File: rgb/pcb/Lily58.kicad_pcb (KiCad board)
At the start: 2 copper layers, 142.5 x 106.3 mm, 117 parts, among them J1 LED, J2 4PIN, P1 i2c_pin, P2 i2c_pin, P3 ICSP, P4 OLED, SW1 SW_PUSH, SW10 SW_PUSH, SW11 SW_PUSH, SW12 SW_PUSH, SW13 SW_PUSH, SW14 SW_PUSH, SW15 SW_PUSH, SW16 SW_PUSH, SW17 SW_PUSH, SW18 SW_PUSH, SW19 SW_PUSH, SW2 SW_PUSH, SW20 SW_PUSH, SW21 SW_PUSH, SW22 SW_PUSH, SW23 SW_PUSH, SW24 SW_PUSH, SW25 SW_PUSH, SW26 SW_PUSH, SW27 SW_PUSH, SW28 SW_PUSH, SW29 SW_PUSH, SW3 SW_PUSH, SW4 SW_PUSH, SW5 SW_PUSH, SW6 SW_PUSH, SW7 SW_PUSH, SW8 SW_PUSH, SW9 SW_PUSH, U1 ProMicro

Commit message: Add underglow
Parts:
- added L30: SK6812mini, Lily58-footprint:SK6812MINI_underglow_rev, F.Cu at (120.5, 60.2)
- added L31: SK6812mini, Lily58-footprint:SK6812MINI_underglow_rev, F.Cu at (158.6, 56.5)
- added L32: SK6812mini, Lily58-footprint:SK6812MINI_underglow_rev, F.Cu at (196.7, 62.6)
- added L33: SK6812mini, Lily58-footprint:SK6812MINI_underglow_rev, F.Cu at (120.5, 117.3)
- added L34: SK6812mini, Lily58-footprint:SK6812MINI_underglow_rev, F.Cu at (158.6, 113.7)
- added L35: SK6812mini, Lily58-footprint:SK6812MINI_underglow_rev, F.Cu at (196.7, 100.8)
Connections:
- L1 pad 3: LED -> Net-(L1-Pad3)
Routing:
- net VCC: track 975.7 -> 1033.8 mm, vias 33 -> 44
- net Net-(L34-Pad1): track 0.00 -> 53.6 mm, vias 0 -> 4
- net Net-(L32-Pad3): track 0.00 -> 49.9 mm, vias 0 -> 3
- net GND: track 1020.5 -> 1070.0 mm, vias 36 -> 45
- net Net-(L31-Pad3): track 0.00 -> 45.2 mm, vias 0 -> 3
- net Net-(L30-Pad3): track 0.00 -> 44.6 mm, vias 0 -> 3
- net Net-(L33-Pad1): track 0.00 -> 43.7 mm, vias 0 -> 4
- net LED: track 85.4 -> 121.3 mm, vias 4 -> 5
- net Net-(L1-Pad3): track 0.00 -> 16.9 mm, vias 0 -> 3
- net col3: track 296.7 -> 300.9 mm
- net col1: track 382.8 -> 385.4 mm
- net col4: track 288.4 -> 290.3 mm
- net col2: track 316.0 -> 314.4 mm
- net col5: track 213.9 -> 215.5 mm
- net row0: track 151.0 -> 149.6 mm
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
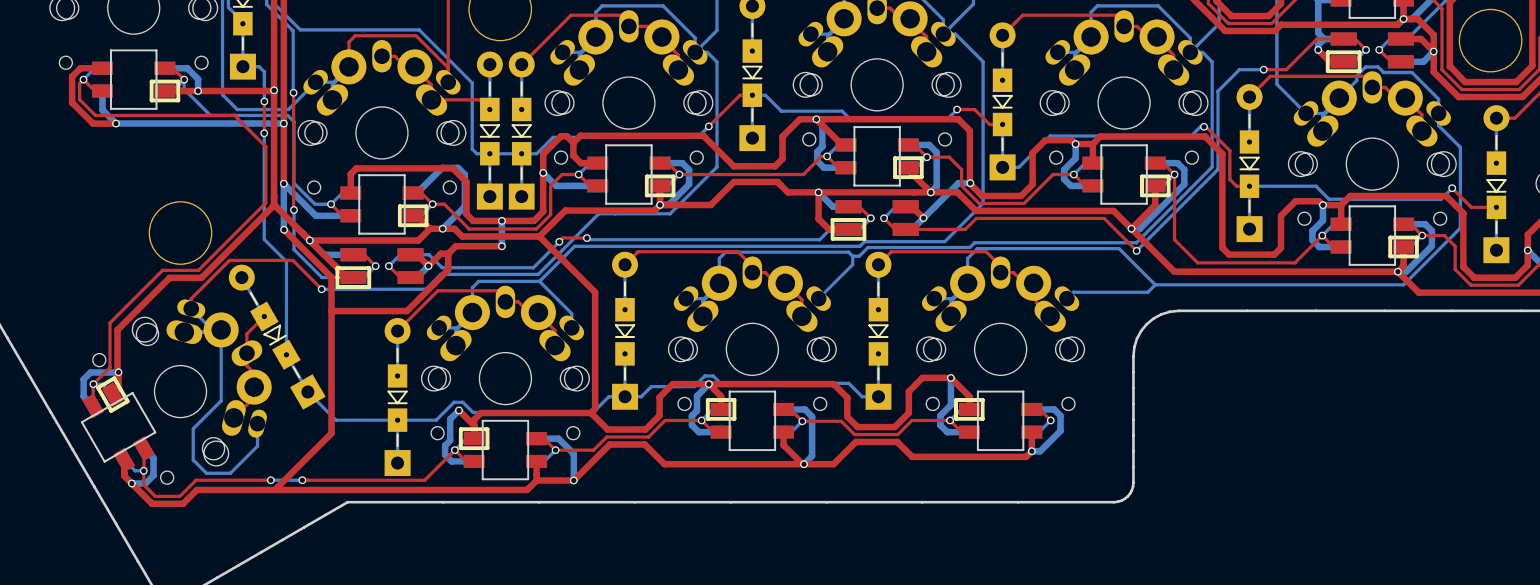
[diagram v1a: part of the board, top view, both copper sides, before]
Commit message: Clean up routing new thumb key
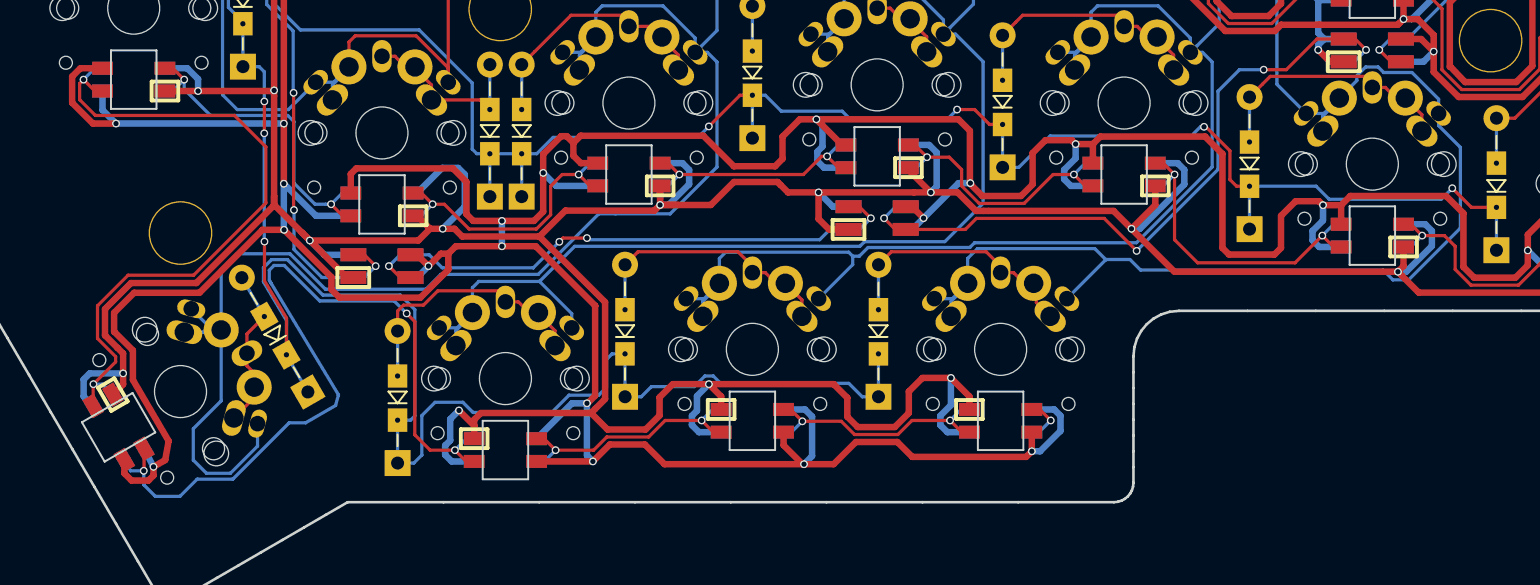
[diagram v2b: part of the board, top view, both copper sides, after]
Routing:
- net Net-(L26-Pad1): track 34.2 -> 64.0 mm, vias 4 -> 3
- net row4: track 139.0 -> 167.1 mm, vias 4 -> 5
- net VCC: track 1033.8 -> 1037.4 mm
- net col1: track 385.4 -> 382.1 mm
- net Net-(L25-Pad1): track 50.0 -> 52.5 mm
- net GND: track 1070.0 -> 1068.1 mm, vias 45 -> 46
- net col4: track 290.3 -> 291.3 mm, vias 1 -> 0
- net Net-(D27-Pad2): track 19.6 -> 20.5 mm

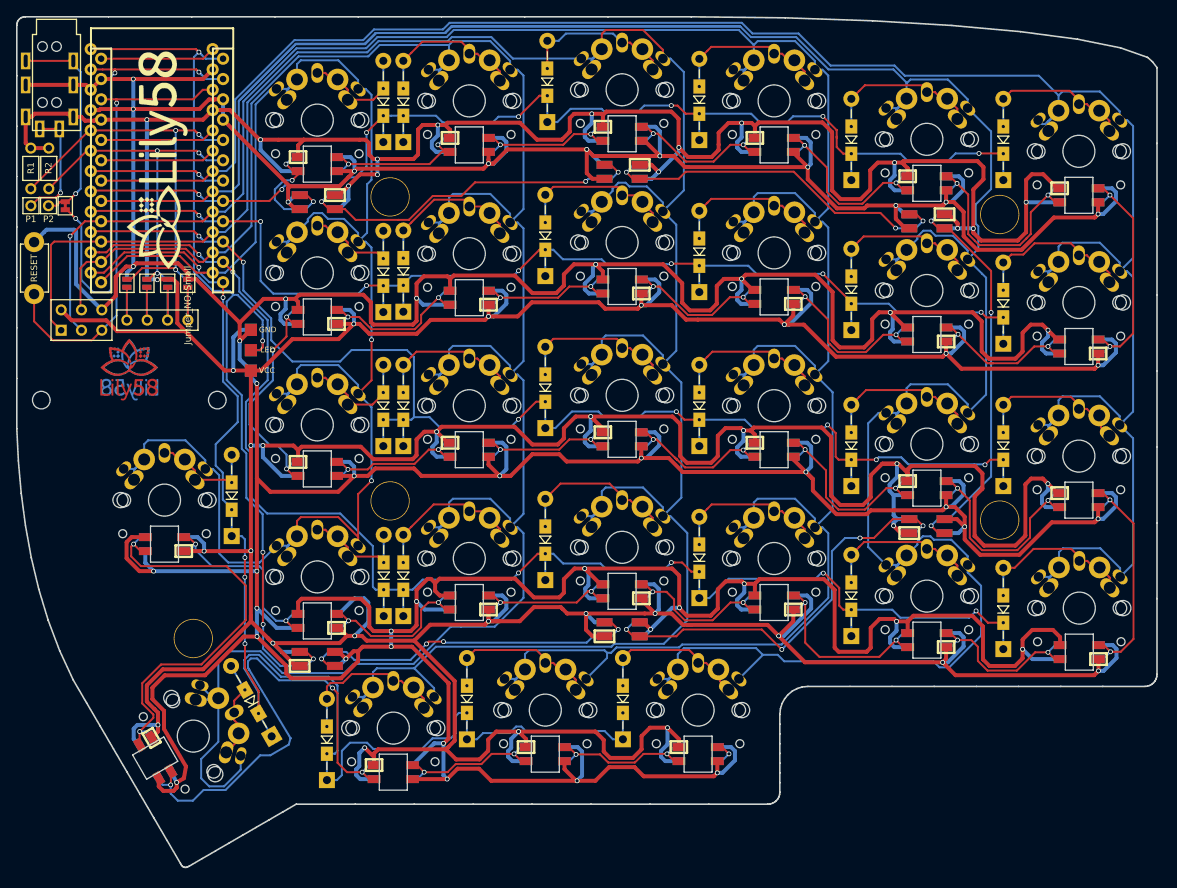
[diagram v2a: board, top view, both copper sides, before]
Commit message: Add ground planes
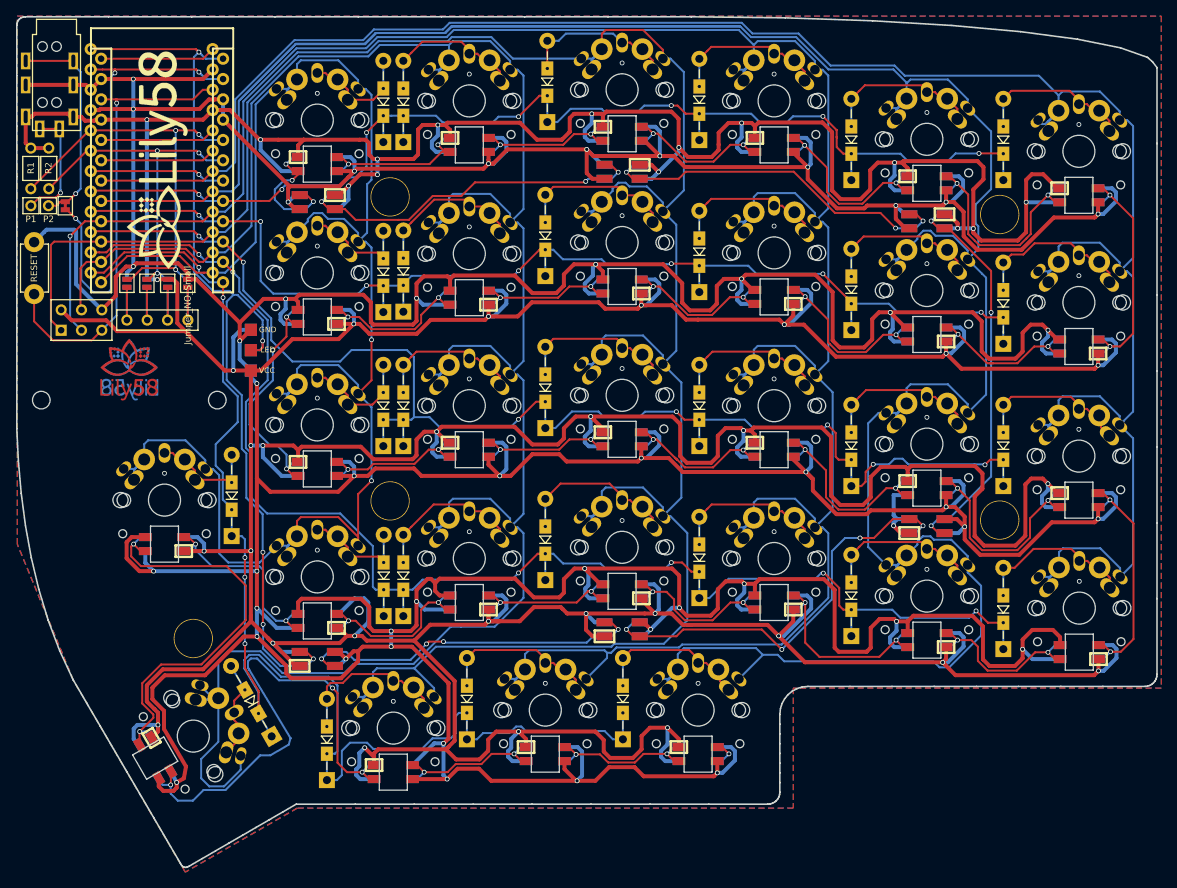
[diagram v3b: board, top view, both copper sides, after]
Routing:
- net VCC: track 1037.4 -> 1030.4 mm, vias 44 -> 43
- net row2: track 166.1 -> 167.2 mm
- net GND: vias 46 -> 74
- added copper zone on B.Cu, net GND
- added copper zone on F.Cu, net GND

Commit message: Add some branding
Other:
- board text added: "Glow"
- board text added: "Lily58 × qtkb"
